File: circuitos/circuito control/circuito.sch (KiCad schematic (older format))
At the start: 27 parts, among them CON1 SD_Card, IC1 ATMEGA328-P, P1 CONN_5V, P2 CONN_02X03, P3 CONN_UART_USB, P4 CONN_UART, SW1 B_RST_N_O, SW2 B_SEL_N_O, SW3 B_CHG_N_O, Y1 16Mhz

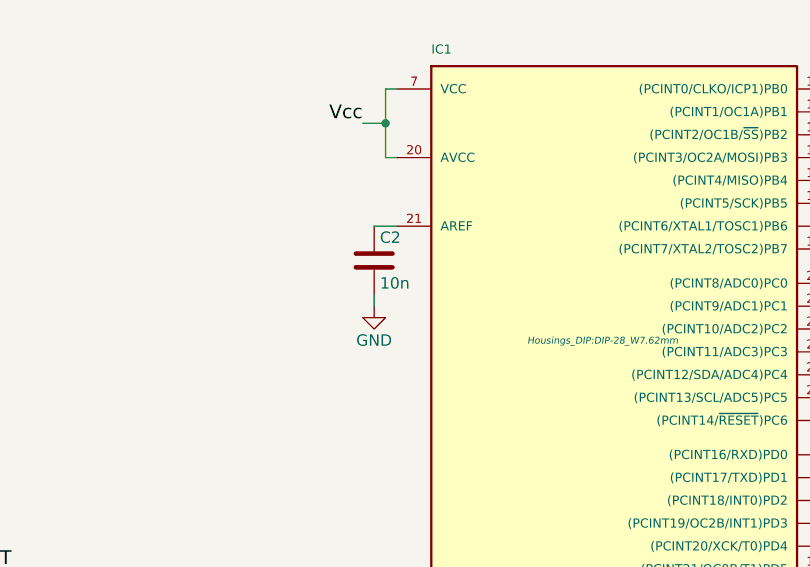
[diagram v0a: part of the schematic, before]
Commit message: cambios esquematicos varios
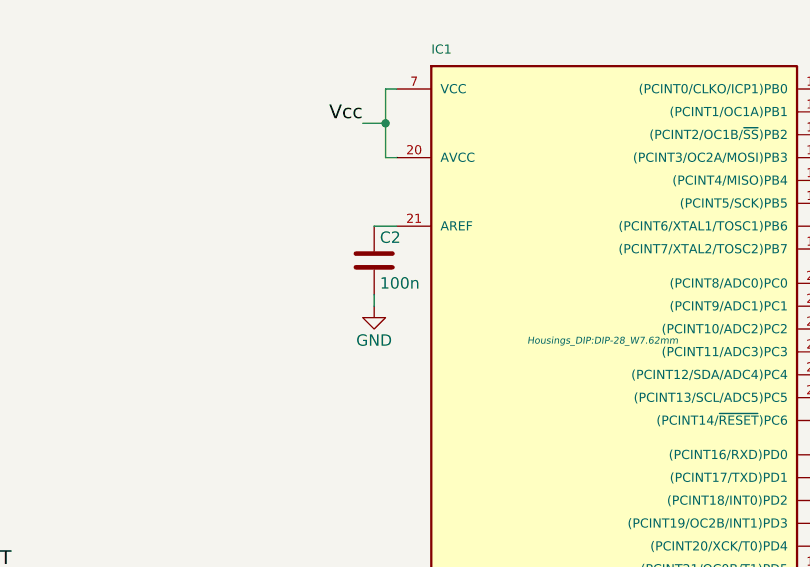
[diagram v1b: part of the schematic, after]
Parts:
- C2: value 10n -> 100n
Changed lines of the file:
@@
 P 4400 2400
 F 0 "C2" H 4425 2500 50  0000 L CNN
-F 1 "10n" H 4425 2300 50  0000 L CNN
+F 1 "100n" H 4425 2300 50  0000 L CNN
 F 2 "Capacitors_ThroughHole:C_Disc_D3_P2.5" H 4438 2250 30  0001 C CNN
 F 3 "" H 4400 2400 60  0000 C CNN

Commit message: adapto graficos para el informe
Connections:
- net RX_USB: now also IC1.6 ((PCINT20/XCK/T0)PD4); no longer IC1.3 ((PCINT17/TXD)PD1)
- net Rx_int: now also IC1.2 ((PCINT16/RXD)PD0); no longer IC1.5 ((PCINT19/OC2B/INT1)PD3)
- net Rx_pc: now also IC1.5 ((PCINT19/OC2B/INT1)PD3); no longer IC1.2 ((PCINT16/RXD)PD0)
- net Tx_int: now also IC1.3 ((PCINT17/TXD)PD1); no longer IC1.6 ((PCINT20/XCK/T0)PD4)
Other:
- moved on the sheet: C1, C2, C3, C4, CON1, D1, D2, DS1, IC1, P1, P2, P3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
